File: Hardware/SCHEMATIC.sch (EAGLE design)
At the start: 105 parts, among them IC1 BQ25180YBGR, IC2 DRV2605YZFR, IC3 BMA421, IC9 RT6160AWSC, J1 503480-2400, J2 TC2030-IDC, J4 KH-TYPE-C-16P, Q1 20V/4.2A/52mΩ/1.4W, Q3 SI1308EDL-T1-GE3, U1 NRF52840 _QF, U3 MAX17048G+T10, X1 32MHz, X2 32.768KHz

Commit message: Remade Schematic + PCB
Remade schematic and started on PCB a bit
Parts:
- removed ANT1: 2450AT18B100E, InkTime_v5:2450AT18B100E_2450AT18B100E
- removed D3: USBLC6-2SC6Y, InkTime_v5:ESP32_C6_LIBRARY_3_USBLC6-2SC6Y
- removed IC3: BMA421, InkTime_v5:BMA423_BMA423
- removed IC9: RT6160AWSC, InkTime_v5:RT6160AWSC_RT6160AWSC
- removed J4: KH-TYPE-C-16P, InkTime_v5:KH-TYPE-C-16P_KH-TYPE-C-16P
- removed L7: FTC252012SR47MBCA, InkTime_v5:MLP2016SR47MT0S1_FTC252012SR47MBCA
- removed U3: MAX17048G+T10, InkTime_v5:ESP32_C6_LIBRARY_MAX17048G+T10
- added ANT2: 2450AT18B100E_2450AT18B100E, InkTime_v5:2450AT18B100E_2450AT18B100E
- added D1: ESP32_C6_LIBRARY_3_USBLC6-2SC6Y, InkTime_v5:ESP32_C6_LIBRARY_3_USBLC6-2SC6Y
- added IC4: BMA423_BMA423, InkTime_v5:BMA423_BMA423
- added IC5: DRV2605YZFR_DRV2605YZFR, InkTime_v5:DRV2605YZFR_DRV2605YZFR
- added J3: 503480-2400_503480-2400, InkTime_v5:503480-2400_503480-2400
- added L4: 15nH, InkTime_v5:MLP2016SR47MT0S1_FTC252012SR47MBCA
- added U$1: NORDIC_NRF_4_NRF52840_QF, InkTime_v5:NORDIC_NRF_4_NRF52840_QF
- IC1: value BQ25180YBGR -> RT6160AWSC_RT6160AWSC; device InkTime_v5:BQ25180YBGR_BQ25180YBGR -> InkTime_v5:RT6160AWSC_RT6160AWSC
- IC2: value DRV2605YZFR -> BQ25180YBGR_BQ25180YBGR; device InkTime_v5:DRV2605YZFR_DRV2605YZFR -> InkTime_v5:BQ25180YBGR_BQ25180YBGR
- J1: value 503480-2400 -> TC2030-IDC_TC2030-IDC; device InkTime_v5:503480-2400_503480-2400 -> InkTime_v5:TC2030-IDC_TC2030-IDC
- J2: value TC2030-IDC -> KH-TYPE-C-16P_KH-TYPE-C-16P; device InkTime_v5:TC2030-IDC_TC2030-IDC -> InkTime_v5:KH-TYPE-C-16P_KH-TYPE-C-16P
- L1: value 3.9nH -> MLP2016SR47MT0S1_FTC252012SR47MBCA
- L2: value 10uH -> 3.9nH
- L3: value 15nH -> 10uH
- U1: value NRF52840 _QF -> ESP32_C6_LIBRARY_MAX17048G+T10; device InkTime_v5:NORDIC_NRF_4_NRF52840_QF -> InkTime_v5:ESP32_C6_LIBRARY_MAX17048G+T10; U1 NRF52840 _QF -> (none)
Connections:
- new net N$24: J3.17
- new net N$3: C7.1, U$1.VDD@AD14
- new net N$34: J2.GND
- new net N$35: J2.DP2
- new net N$36: J2.DN2
- new net N$7: IC5.IN/TRIG
- net 3V3/1.7D: now also IC5.VDD; no longer IC2.VDD
- net 3V3/2.4A: now also IC1.VOUT_1, IC1.VOUT_2, IC4.CSB, IC4.VDD, IC4.VDDIO, J1.1, U$1.VDD@AD23, U$1.VDD@W1, U$1.VDDH@Y2; no longer C7.1, IC3.CSB, IC3.VDD, IC3.VDDIO, IC9.VOUT_1, IC9.VOUT_2, J2.1, U1.VDD@AD14, U1.VDD@AD23, U1.VDD@W1, U1.VDDH@Y2
- net ALERT/1.6C: now also U1.!ALERT; no longer U3.!ALERT
- net ALERT/2.5C: now also U$1.P0.10/NFC2@J24; no longer U1.P0.10/NFC2@J24
- net D+/1.5D: now also D1.I/O2_2; no longer D3.I/O2_2
- net D+/2.7D: now also U$1.D+@AD6; no longer U1.D+@AD6
- net D-/1.5D: now also D1.I/O1_2; no longer D3.I/O1_2
- net D-/2.7D: now also U$1.D-@AD4; no longer U1.D-@AD4
- net DEC1: now also U$1.DEC1@C1; no longer U1.DEC1@C1
- net DEC4_6: now also L4.2, U$1.DEC4@B5, U$1.DEC6@E24; no longer L3.2, U1.DEC4@B5, U1.DEC6@E24
- net DN: now also D1.I/O1_1, J2.DN1; no longer D3.I/O1_1, J4.DN1, J4.DN2
- net DP: now also D1.I/O2_1, J2.DP1; no longer D3.I/O2_1, J4.DP1, J4.DP2
- net EPD_3V3: now also J3.15, J3.16; no longer J1.15, J1.16
- net EPD_BUSY/1.5D: now also J3.9; no longer J1.9
- net EPD_BUSY/2.2D: now also U$1.P0.17@AD12; no longer U1.P0.17@AD12
- net EPD_CS/1.4C: now also J3.12; no longer J1.12
- net EPD_CS/2.2D: now also U$1.P0.05/AIN3@K2; no longer U1.P0.05/AIN3@K2
- net EPD_DC/1.5D: now also J3.11; no longer J1.11
- net EPD_DC/2.2D: now also U$1.P0.15@AD10; no longer U1.P0.15@AD10
- net EPD_RST/1.5D: now also J3.10; no longer J1.10
- net EPD_RST/2.2D: now also U$1.P0.16@AC11; no longer U1.P0.16@AC11
- net GDR: now also J3.2; no longer J1.2
- net GND: now also D1.GND, IC1.AGND, IC1.PGND_1, IC1.PGND_2, IC1.VSEL, IC4.GND, IC4.GNDIO, IC5.GND, J1.3, J1.5, J2.SHIELD, J3.8, J3.MP1, J3.MP2, U$1.VSS@B7, U$1.VSS_PA@F23, U$1.VSS_PAD, U1.CTG, U1.EP, U1.GND, U1.QSTRT; no longer D3.GND, IC1.GND, IC2.IN/TRIG, IC3.GND, IC3.GNDIO, IC9.AGND, IC9.PGND_1, IC9.PGND_2, IC9.VSEL, J1.17, J1.8, J1.MP1, J1.MP2, J2.3, J2.5, J4.GND, J4.SHIELD, U1.VSS@B7, U1.VSS_PA@F23, U1.VSS_PAD, U3.CTG, U3.EP, U3.GND, U3.QSTRT
- net HAPTIC_EN/1.4C: now also IC5.EN; no longer IC2.EN
- net HAPTIC_EN/2.6A: now also U$1.P0.12@U1; no longer U1.P0.12@U1
- net IMU_INT1: now also IC4.INT1, U$1.P0.08@N1; no longer IC3.INT1, U1.P0.08@N1
- net IMU_INT2: now also IC4.INT2, U$1.P1.08@P2; no longer IC3.INT2, U1.P1.08@P2
- net LX1: now also IC1.SW1_1, IC1.SW1_2, L1.1; no longer IC9.SW1_1, IC9.SW1_2, L7.1
- net LX2: now also IC1.SW2_1, IC1.SW2_2, L1.2; no longer IC9.SW2_1, IC9.SW2_2, L7.2
- net MOSI/1.5B: now also J3.14; no longer J1.14
- net MOSI/2.2D: now also U$1.P0.03/AIN1@B13; no longer U1.P0.03/AIN1@B13
- net N$1: now also U$1.DEC3@D23; no longer U1.DEC3@D23
- net N$10: now also L3.1, U$1.DCC@B3; no longer L2.1, U1.DCC@B3
- net N$11: now also U$1.P0.22@AD18; no longer U1.P0.22@AD18
- net N$12: now also L3.2, L4.1; no longer L2.2, L3.1
- net N$13: now also U$1.DEC2@A18; no longer U1.DEC2@A18
- net N$14: now also U$1.VDD@A22; no longer U1.VDD@A22
- net N$15: now also IC4.SDO; no longer IC3.SDO
- net N$16: now also IC1.SCL; no longer IC9.SCL
- net N$17: now also IC1.SDA; no longer IC9.SDA
- net N$19: now also IC2.TS/MR; no longer IC1.TS/MR
- net N$2: now also L2.1, U$1.ANT@H23; no longer L1.1, U1.ANT@H23
- net N$23: now also J3.4; no longer J1.4
- net N$25: now also J3.5; no longer J1.5
- net N$26: now also J3.18; no longer J1.18
- net N$27: now also J3.19; no longer J1.19
- net N$28: now also J3.20; no longer J1.20
- net N$29: now also J3.22; no longer J1.22
- net N$30: now also J3.24; no longer J1.24
- net N$31: now also IC5.REG; no longer IC2.REG
- net N$32: now also J2.CC1; no longer J4.CC1
- net N$33: now also J2.CC2; no longer J4.CC2
- net N$4: now also U$1.XC1@B24; no longer U1.XC1@B24
- net N$5: now also U$1.XC2@A23; no longer U1.XC2@A23
- net N$6: now also U$1.DEC3V3@AC5; no longer U1.DEC3V3@AC5
- net N$8: now also U$1.DEC5@N24; no longer U1.DEC5@N24
- net N$9: now also U$1.VDD@B1; no longer U1.VDD@B1
- net OUT: now also IC5.OUT-; no longer IC2.OUT-
- net OUT+: now also IC5.OUT+; no longer IC2.OUT+
- net P0.00/XL1: now also U$1.P0.00/XL1@D2; no longer U1.P0.00/XL1@D2
- net P0.01/XL2: now also U$1.P0.01/XL2@F2; no longer U1.P0.01/XL2@F2
- net P0.04: now also U$1.P0.04/AIN2@J1; no longer U1.P0.04/AIN2@J1
- net P0.09: now also U$1.P0.09/NFC1@L24; no longer U1.P0.09/NFC1@L24
- net P0.26: now also U$1.P0.26@G1; no longer U1.P0.26@G1
- net P0.27: now also U$1.P0.27@H2; no longer U1.P0.27@H2
- net P0.28: now also U$1.P0.28/AIN4@B11; no longer U1.P0.28/AIN4@B11
- net P0.29: now also U$1.P0.29/AIN5@A10; no longer U1.P0.29/AIN5@A10
- net P0.30: now also U$1.P0.30/AIN6@B9; no longer U1.P0.30/AIN6@B9
- net P0.31: now also U$1.P0.31/AIN7@A8; no longer U1.P0.31/AIN7@A8
- net P1.01/2.4B: now also U$1.P1.01@Y23; no longer U1.P1.01@Y23
- net P1.02/2.8C: now also U$1.P1.02@W24; no longer U1.P1.02@W24
- net P1.03: now also U$1.P1.03@V23; no longer U1.P1.03@V23
- net P1.04: now also U$1.P1.04@U24; no longer U1.P1.04@U24
- net P1.05: now also U$1.P1.05@T23; no longer U1.P1.05@T23
- net P1.06: now also U$1.P1.06@R24; no longer U1.P1.06@R24
- net P1.07: now also U$1.P1.07@P23; no longer U1.P1.07@P23
- net P1.09: now also U$1.P1.09@R1; no longer U1.P1.09@R1
- net P1.10: now also U$1.P1.10@A20; no longer U1.P1.10@A20
- net P1.11: now also U$1.P1.11@B19; no longer U1.P1.11@B19
- net P1.12: now also U$1.P1.12@B17; no longer U1.P1.12@B17
- net P1.13: now also U$1.P1.13@A16; no longer U1.P1.13@A16
- net P1.14: now also U$1.P1.14@B15; no longer U1.P1.14@B15
- net P1.15: now also U$1.P1.15@A14; no longer U1.P1.15@A14
- net PMIC_INT: now also IC2.!INT, U$1.P0.11@T2; no longer IC1.!INT, U1.P0.11@T2
- net PO.13/2.6C: now also U$1.P0.13@AD8; no longer U1.P0.13@AD8
- net PO.14/2.7C: now also U$1.P0.14@AC9; no longer U1.P0.14@AC9
- net PO.19: now also U$1.P0.19@AC15; no longer U1.P0.19@AC15
- net PO.20: now also U$1.P0.20@AD16; no longer U1.P0.20@AD16
- net PO.21: now also U$1.P0.21@AC17; no longer U1.P0.21@AC17
- net PO.22: now also U$1.P0.23@AC19; no longer U1.P0.23@AC19
- net PO.24: now also U$1.P0.24@AD20; no longer U1.P0.24@AD20
- net PO.25: now also U$1.P0.25@AC21; no longer U1.P0.25@AC21
- net PREVGH: now also J3.21; no longer J1.21
- net PREVGL: now also J3.23; no longer J1.23
- net RESE: now also J3.3; no longer J1.3
- net RESET: now also J1.6, U$1.P0.18/RESET@AC13; no longer J2.6, U1.P0.18/RESET@AC13
- net RF: now also ANT2.FEED, L2.2; no longer ANT1.FEED, L1.2
- net SCK/1.5B: now also J3.13; no longer J1.13
- net SCK/2.2D: now also U$1.P0.02/AIN0@A12; no longer U1.P0.02/AIN0@A12
- net SCL/1.4C: now also IC5.SCL; no longer IC2.SCL
- net SCL/2.4C: now also IC2.SCL, IC4.SCX, U$1.P0.07@M2, U1.SCL; no longer IC1.SCL, U1.P0.07@M2, U3.SCL
- net SDA/1.4C: now also IC5.SDA; no longer IC2.SDA
- net SDA/2.4C: now also IC2.SDA, IC4.SDX, U$1.P0.06@L1, U1.SDA; no longer IC1.SDA, IC3.SDX, U1.P0.06@L1, U3.SDA
- net SWDCLK: now also J1.4, U$1.SWDCLK@AA24; no longer J2.4, U1.SWDCLK@AA24
- net SWDIO: now also J1.2, U$1.SWDIO@AC24; no longer J2.2, U1.SWDIO@AC24
- net SWO: now also U$1.P1.00@AD22; no longer U1.P1.00@AD22
- net VBAT/1.2A: now also U1.CELL, U1.VDD; no longer U3.CELL, U3.VDD
- net VBAT/2.5C: now also IC2.BAT; no longer IC1.BAT
- net VBUS/1.5D: now also D1.VBUS, J2.VBUS; no longer D3.VBUS, J4.VBUS
- net VBUS/2.6D: now also IC2.IN, U$1.VBUS@AD2; no longer IC1.IN, U1.VBUS@AD2
- net VREG: now also IC1.EN, IC1.VIN_1, IC1.VIN_2, IC2.SYS; no longer IC1.SYS, IC9.EN, IC9.VIN_1, IC9.VIN_2
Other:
- note added: "Drawn by: Andrei-Alexandru Rusu"
- note added: "InkTime V6"
- note added: "LiPo Charger"
- note removed: "InkTime v6"
- note removed: "LIPo Charger"
- note removed: "drawn by: Andrei-Alexandru Rusu"
- moved on the sheet: C1, C1-EP-DR, C10, C11, C12, C13, C14, C15, C16, C17, C18, C19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

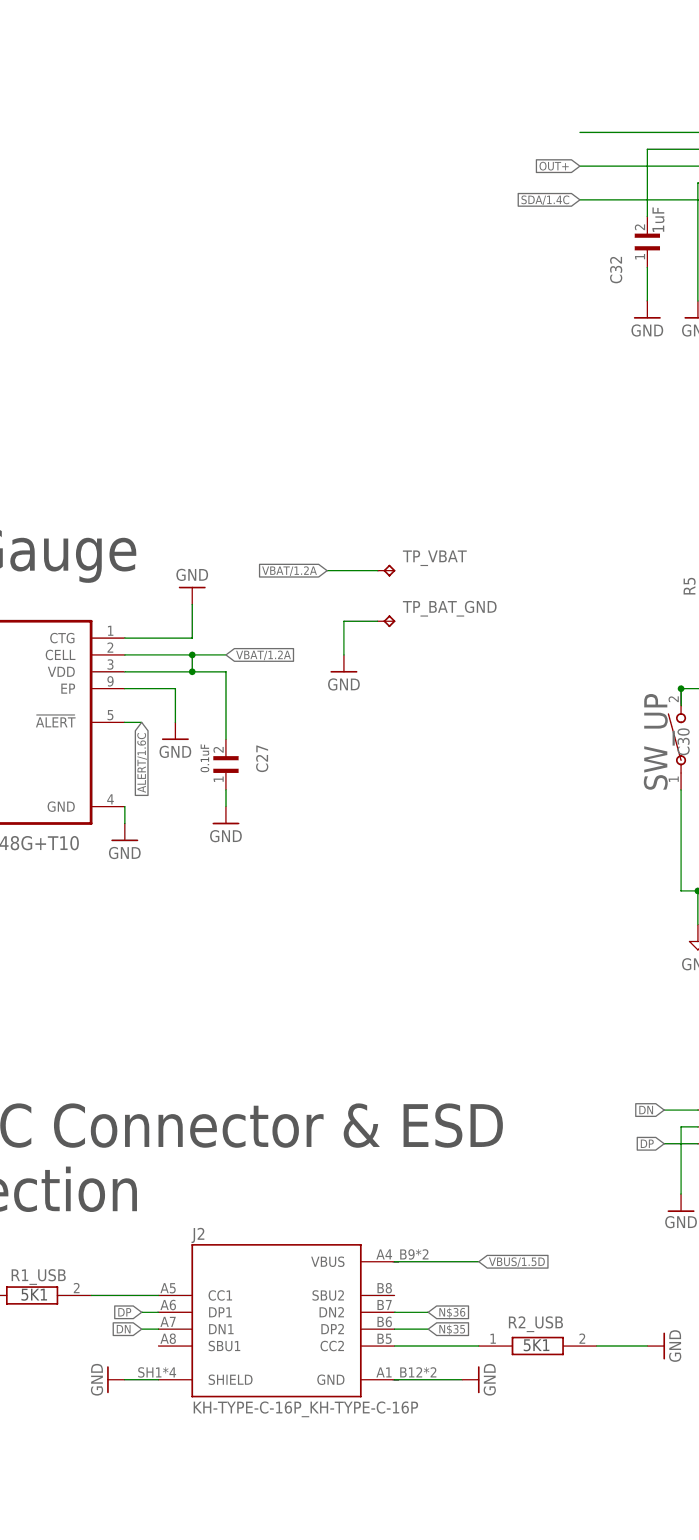
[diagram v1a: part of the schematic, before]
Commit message: Add some of the missing files and edits from PCB and Schematic
Added some images, edited out the schematic a bit added a 3D model for the USB. Also added Gerbers and BOM
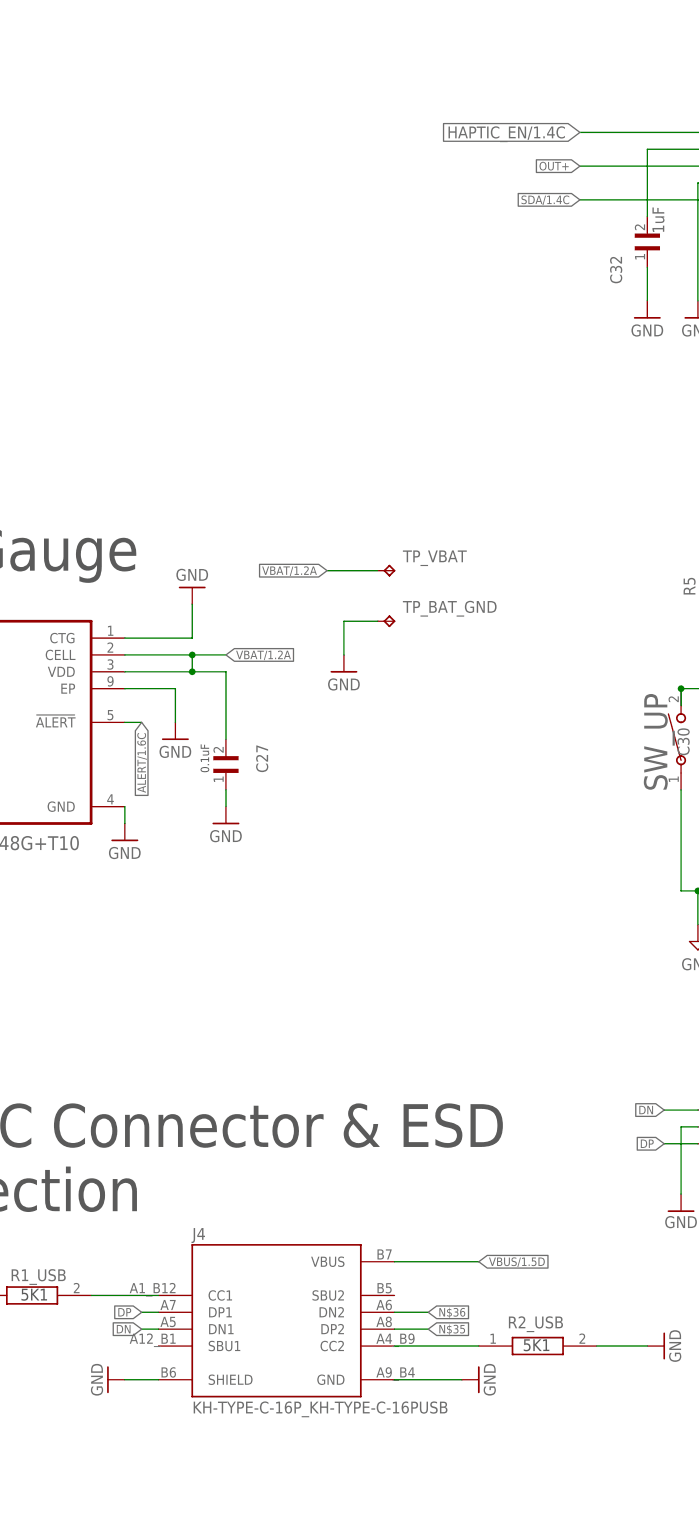
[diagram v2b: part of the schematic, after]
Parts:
- removed J2: KH-TYPE-C-16P_KH-TYPE-C-16P, InkTime_v5:KH-TYPE-C-16P_KH-TYPE-C-16P
- added J4: KH-TYPE-C-16P_KH-TYPE-C-16PUSB, InkTime_v5:KH-TYPE-C-16P_KH-TYPE-C-16PUSB
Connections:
- net DN: now also J4.DN1; no longer J2.DN1
- net DP: now also J4.DP1; no longer J2.DP1
- net GND: now also J4.SHIELD; no longer J2.SHIELD
- net N$32: now also J4.CC1; no longer J2.CC1
- net N$33: now also J4.CC2; no longer J2.CC2
- net N$34: now also J4.GND; no longer J2.GND
- net N$35: now also J4.DP2; no longer J2.DP2
- net N$36: now also J4.DN2; no longer J2.DN2
- net VBUS/1.5D: now also J4.VBUS; no longer J2.VBUS
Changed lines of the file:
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@@
 <part name="C43" library="InkTime_v5" library_urn="urn:adsk.wipprod:fs.file:vf.UGCviqsKRuyr22hNdtfhcA" deviceset="NORDIC_NRF_3_CAPACITOR" device="_0402_L" value="4.7uF\"/>
 <part name="SUPPLY61" library="InkTime_v5" library_urn="urn:adsk.wipprod:fs.file:vf.UGCviqsKRuyr22hNdtfhcA" deviceset="TUTORIAL---FUSION-360_GND-BAR" device="" value="GND"/>
-<part name="J2" library="InkTime_v5" library_urn="urn:adsk.wipprod:fs.file:vf.FTfBbUvaT7WQPpG4NnEaNQ" deviceset="KH-TYPE-C-16P_KH-TYPE-C-16P" device=""/>
 <part name="D1" library="InkTime_v5" library_urn="urn:adsk.wipprod:fs.file:vf.FTfBbUvaT7WQPpG4NnEaNQ" deviceset="ESP32_C6_LIBRARY_3_USBLC6-2SC6Y" device=""/>
+<part name="J4" library="InkTime_v5" library_urn="urn:adsk.wipprod:fs.file:vf.FTfBbUvaT7WQPpG4NnEaNQ" deviceset="KH-TYPE-C-16P_KH-TYPE-C-16P" device="USB"/>
 </parts>
 <sheets>
@@
 <attribute name="VALUE" x="-93.98" y="-220.98" size="1.778" layer="96" align="bottom-center"/>
 </instance>
-<instance part="J2" gate="G$1" x="-177.8" y="-210.82" smashed="yes">
-<attribute name="NAME" x="-190.5" y="-199.898" size="1.778" layer="95"/>
-<attribute name="VALUE" x="-190.5" y="-226.06" size="1.778" layer="96"/>
-</instance>
 <instance part="D1" gate="G$1" x="-114.3" y="-180.34" smashed="yes">
 <attribute name="NAME" x="-85.09" y="-172.72" size="1.778" layer="95" align="center-left"/>
 <attribute name="VALUE" x="-85.09" y="-175.26" size="1.778" layer="96" align="center-left"/>
+</instance>
+<instance part="J4" gate="G$1" x="-177.8" y="-210.82" smashed="yes">
+<attribute name="NAME" x="-190.5" y="-199.898" size="1.778" layer="95"/>
+<attribute name="VALUE" x="-190.5" y="-226.06" size="1.778" layer="96"/>
 </instance>
 </instances>
@@
 <wire x1="-195.58" y1="-220.98" x2="-200.66" y2="-220.98" width="0.1524" layer="91"/>
 <pinref part="SUPPLY57" gate="G$1" pin="GND"/>
-<pinref part="J2" gate="G$1" pin="SHIELD"/>
+<pinref part="J4" gate="G$1" pin="SHIELD"/>
 </segment>
 <segment>
@@
 <wire x1="-111.76" y1="-33.02" x2="-132.08" y2="-33.02" width="0.1524" layer="91"/>
 <pinref part="IC5" gate="G$1" pin="EN"/>
+<label x="-132.08" y="-33.02" size="1.778" layer="95" rot="R180" xref="yes"/>
 </segment>
 </net>
@@
 <wire x1="-195.58" y1="-208.28" x2="-205.74" y2="-208.28" width="0.1524" layer="91"/>
 <pinref part="R1_USB" gate="G$1" pin="2"/>
-<pinref part="J2" gate="G$1" pin="CC1"/>
+<pinref part="J4" gate="G$1" pin="CC1"/>
 </segment>
 </net>
@@
 <wire x1="-195.58" y1="-210.82" x2="-198.12" y2="-210.82" width="0.1524" layer="91"/>
 <label x="-198.12" y="-210.82" size="1.27" layer="95" rot="R180" xref="yes"/>
-<pinref part="J2" gate="G$1" pin="DP1"/>
+<pinref part="J4" gate="G$1" pin="DP1"/>
 </segment>
 <segment>
@@
 <wire x1="-195.58" y1="-213.36" x2="-198.12" y2="-213.36" width="0.1524" layer="91"/>
 <label x="-198.12" y="-213.36" size="1.27" layer="95" rot="R180" xref="yes"/>
-<pinref part="J2" gate="G$1" pin="DN1"/>
+<pinref part="J4" gate="G$1" pin="DN1"/>
 </segment>
 <segment>
@@
 <wire x1="-160.02" y1="-203.2" x2="-147.32" y2="-203.2" width="0.1524" layer="91"/>
 <label x="-147.32" y="-203.2" size="1.27" layer="95" xref="yes"/>
-<pinref part="J2" gate="G$1" pin="VBUS"/>
+<pinref part="J4" gate="G$1" pin="VBUS"/>
 </segment>
 <segment>
@@
 <wire x1="-160.02" y1="-215.9" x2="-147.32" y2="-215.9" width="0.1524" layer="91"/>
 <pinref part="R2_USB" gate="G$1" pin="1"/>
-<pinref part="J2" gate="G$1" pin="CC2"/>
+<pinref part="J4" gate="G$1" pin="CC2"/>
 </segment>
 </net>
@@
 <pinref part="SUPPLY59" gate="G$1" pin="GND"/>
 <wire x1="-160.02" y1="-220.98" x2="-149.86" y2="-220.98" width="0.1524" layer="91"/>
-<pinref part="J2" gate="G$1" pin="GND"/>
+<pinref part="J4" gate="G$1" pin="GND"/>
 </segment>
 </net>
@@
 <wire x1="-160.02" y1="-213.36" x2="-154.94" y2="-213.36" width="0.1524" layer="91"/>
 <label x="-154.94" y="-213.36" size="1.27" layer="95" xref="yes"/>
-<pinref part="J2" gate="G$1" pin="DP2"/>
+<pinref part="J4" gate="G$1" pin="DP2"/>
 </segment>
 </net>
@@
 <wire x1="-160.02" y1="-210.82" x2="-154.94" y2="-210.82" width="0.1524" layer="91"/>
 <label x="-154.94" y="-210.82" size="1.27" layer="95" xref="yes"/>
-<pinref part="J2" gate="G$1" pin="DN2"/>
-</segment>
-</net>
+<pinref part="J4" gate="G$1" pin="DN2"/>
+</segment>
+</net>
